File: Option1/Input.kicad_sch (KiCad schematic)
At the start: 1 part, among them J503 KF2EDGKRG-3.5-2*7P

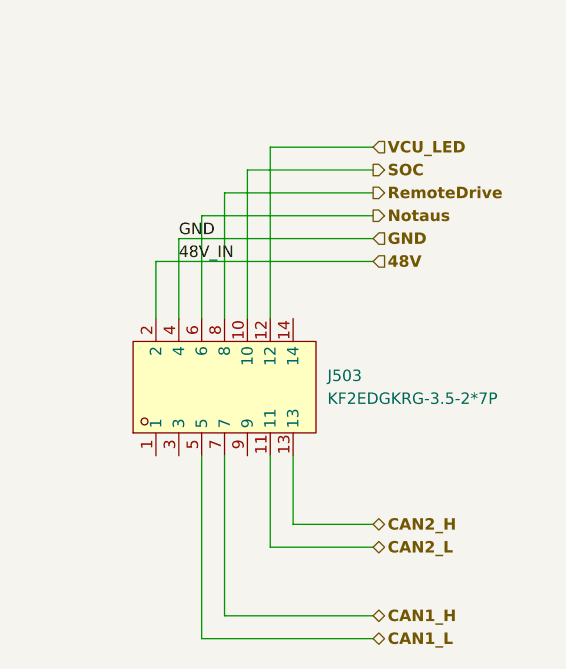
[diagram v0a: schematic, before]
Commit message: Platine korrigeiert, 5V DCDC getauscht, 3.3V Display Versorgung entfernt. Bauteile neu angeordnet, USB 5V auf 5V Supply geführt
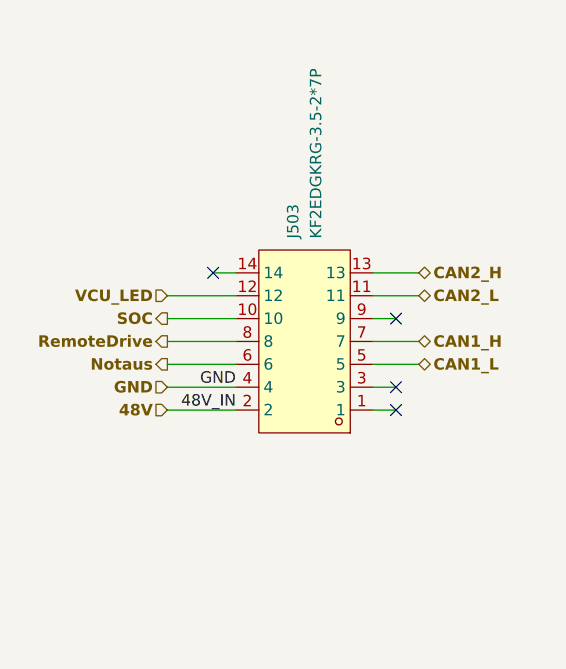
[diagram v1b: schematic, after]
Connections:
- net 48V: no longer J503.4
- new net GND: J503.4
- no-connect marks 0 -> 4
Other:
- moved on the sheet: J503

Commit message: power Supply angepasst für 12V und 48V, Datenblätter für DCDCs hinzugefügt
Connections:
- net 48V renamed V_IN
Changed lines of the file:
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@@
 		)
 	)
-	(hierarchical_label "48V"
+	(hierarchical_label "V_IN"
 		(shape input)
 		(at 31.75 78.74 180)
